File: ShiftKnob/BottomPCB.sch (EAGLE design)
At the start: 37 parts, among them IC2 7805DT, Q1 16MHz, Q2 MOSFET-NCHANNELSMD, Q3 MOSFET-PCHANNELSMD, Q4 MOSFET-NCHANNELSMD, Q5 MOSFET-NCHANNELSMD, Q6 MOSFET-NCHANNELSMD, U1 ATMEGA328

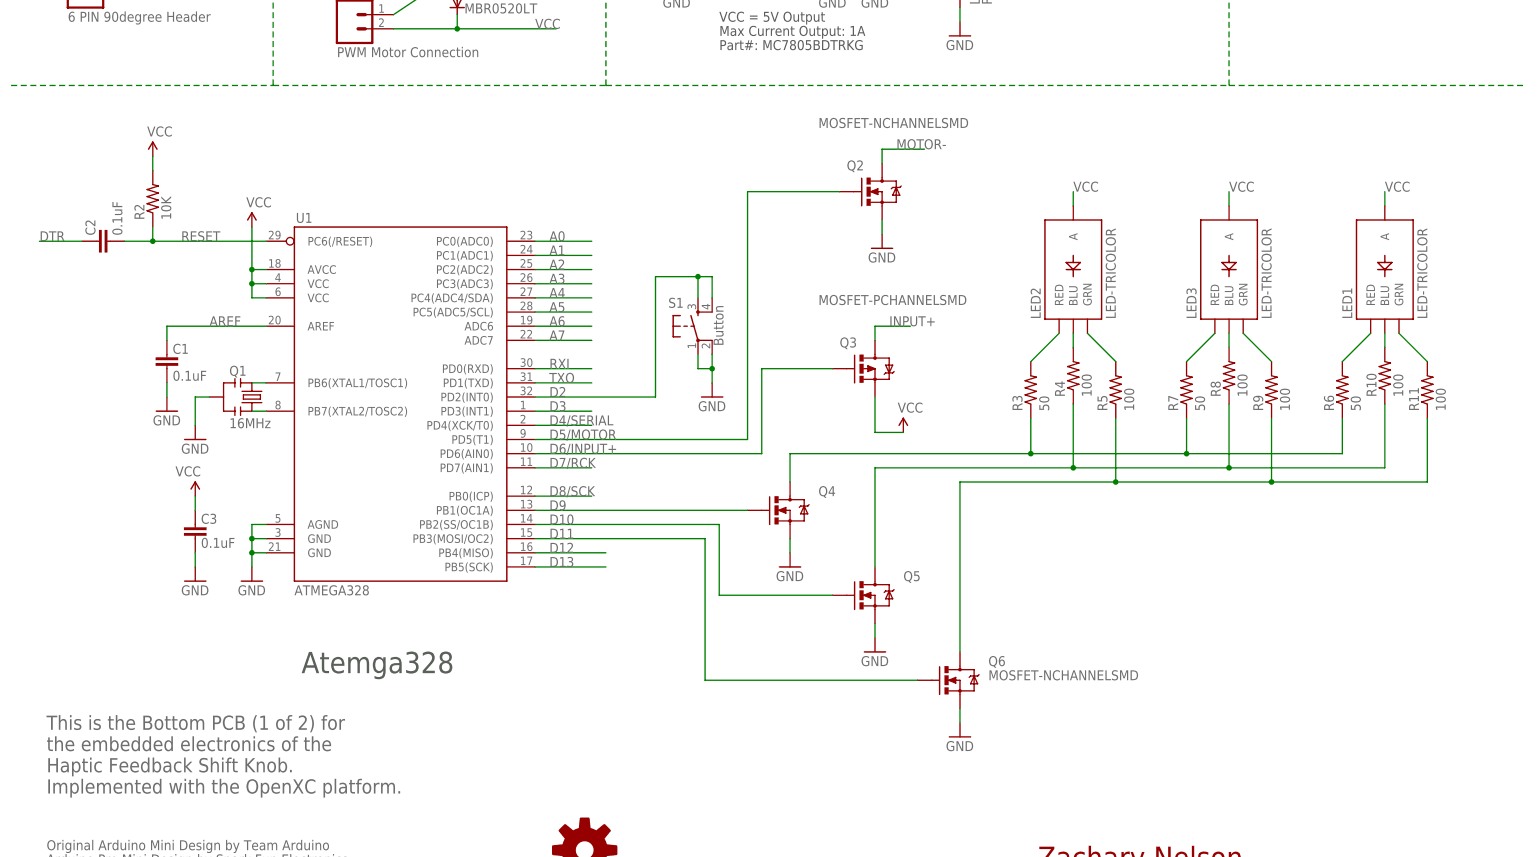
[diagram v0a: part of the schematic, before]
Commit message: add ICSP 6-pin header to schematic.
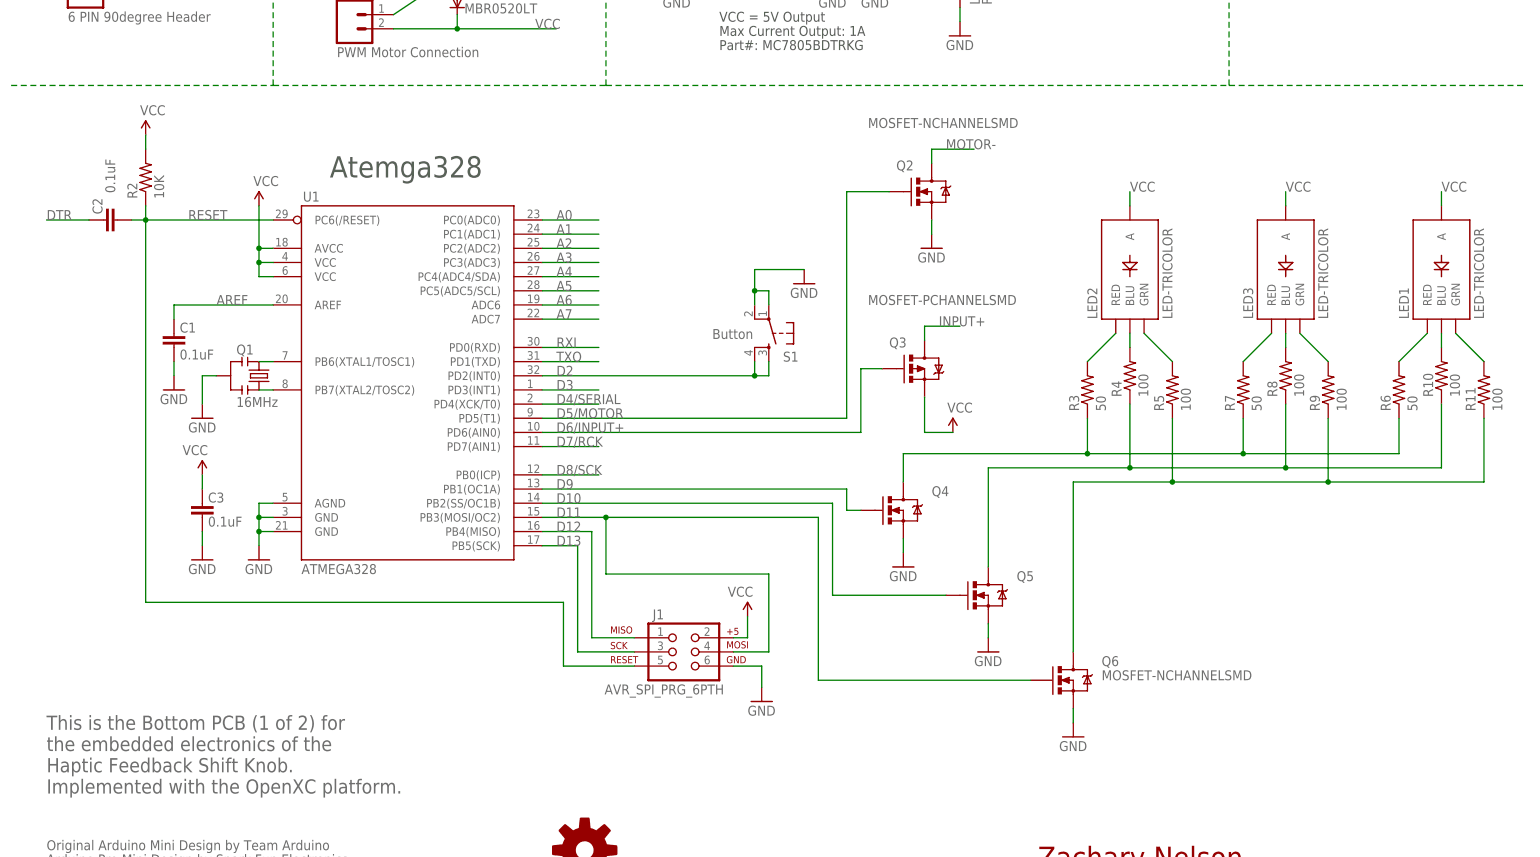
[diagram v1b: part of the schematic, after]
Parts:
- added J1: AVR_SPI_PRG_6PTH, SparkFun-Connectors:AVR_SPI_PRG_6PTH
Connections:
- net D12: now also J1.1
- net D13: now also J1.3
- net GND: now also J1.6
- net N$15: now also J1.4
- net RESET: now also J1.5
- net VCC: now also J1.2
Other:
- moved on the sheet: C1, C2, C3, LED1, LED2, LED3, Q1, Q2, Q3, Q4, Q5, Q6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

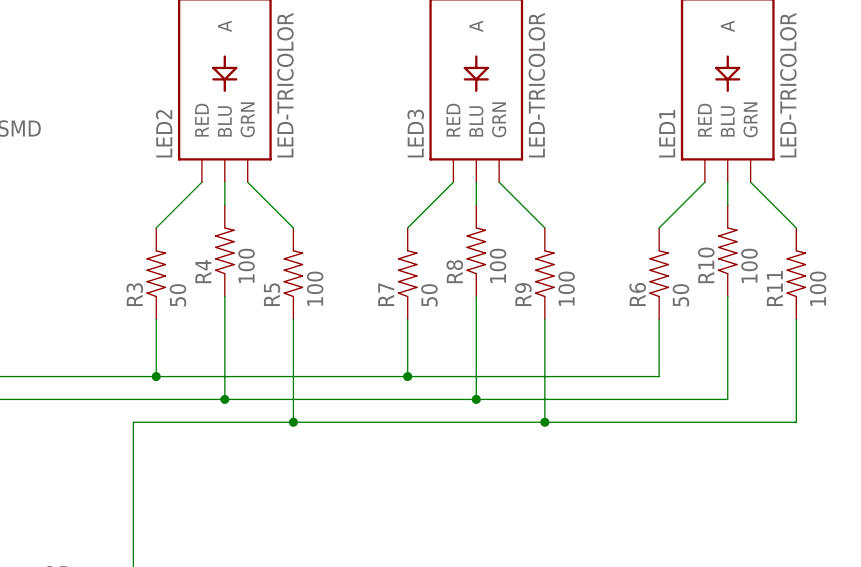
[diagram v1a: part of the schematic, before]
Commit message: change red LED resistance from 50ohm to 100ohm.
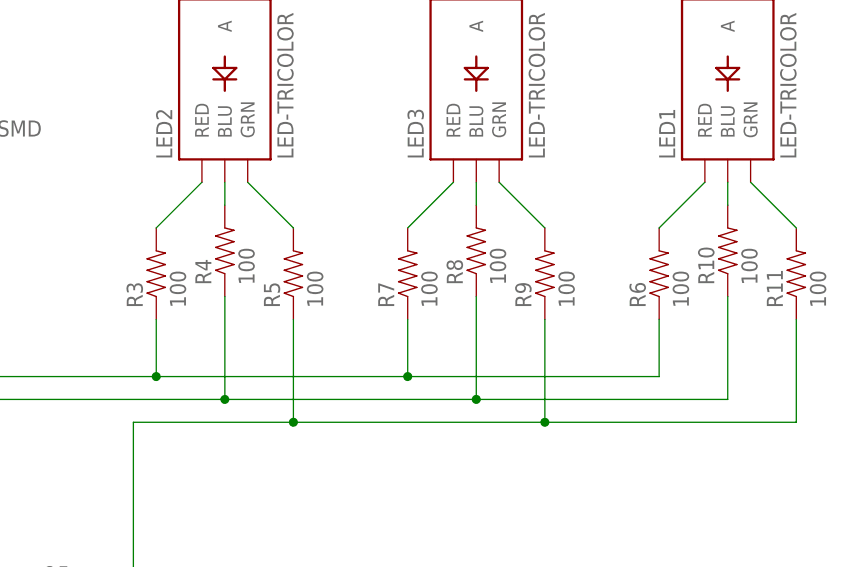
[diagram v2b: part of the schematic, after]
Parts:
- R3, R6, R7: value 50 -> 100
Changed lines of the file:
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@@
 <part name="GND11" library="SparkFun" deviceset="GND" device=""/>
 <part name="R4" library="SparkFun-Resistors" deviceset="RESISTOR" device="0805-RES" value="100"/>
-<part name="R3" library="SparkFun-Resistors" deviceset="RESISTOR" device="0805-RES" value="50"/>
+<part name="R3" library="SparkFun-Resistors" deviceset="RESISTOR" device="0805-RES" value="100"/>
 <part name="R5" library="SparkFun-Resistors" deviceset="RESISTOR" device="0805-RES" value="100"/>
-<part name="R7" library="SparkFun-Resistors" deviceset="RESISTOR" device="0805-RES" value="50"/>
+<part name="R7" library="SparkFun-Resistors" deviceset="RESISTOR" device="0805-RES" value="100"/>
 <part name="R8" library="SparkFun-Resistors" deviceset="RESISTOR" device="0805-RES" value="100"/>
 <part name="R9" library="SparkFun-Resistors" deviceset="RESISTOR" device="0805-RES" value="100"/>
@@
 <part name="D1" library="diode" deviceset="MBR0520LT" device=""/>
 <part name="LED1" library="SparkFun" deviceset="LED-TRICOLOR" device=""/>
-<part name="R6" library="SparkFun-Resistors" deviceset="RESISTOR" device="0805-RES" value="50"/>
+<part name="R6" library="SparkFun-Resistors" deviceset="RESISTOR" device="0805-RES" value="100"/>
 <part name="R10" library="SparkFun-Resistors" deviceset="RESISTOR" device="0805-RES" value="100"/>
 <part name="R11" library="SparkFun-Resistors" deviceset="RESISTOR" device="0805-RES" value="100"/>

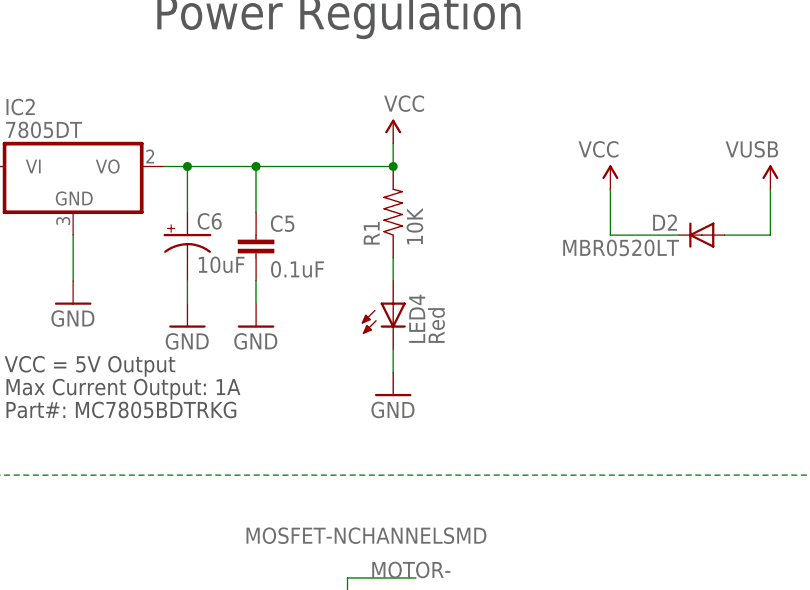
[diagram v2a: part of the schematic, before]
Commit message: remove power LED and resistor. not needed as RGB leds turn on when 5V is applied during startup.
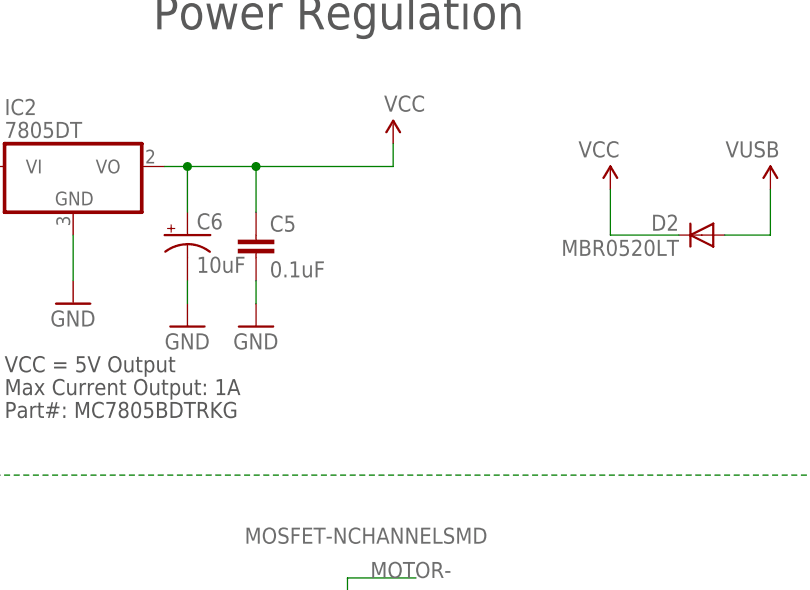
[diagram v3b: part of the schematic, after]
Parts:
- removed LED4: Red, SparkFun:LED0603
- removed R1: 10K, SparkFun:RESISTOR0402-RES
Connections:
- removed net N$3: LED4.A, R1.1
- net GND: no longer LED4.C
- net VCC: no longer R1.2
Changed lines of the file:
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@@
 <part name="GND9" library="SparkFun" deviceset="GND" device=""/>
 <part name="GND10" library="SparkFun" deviceset="GND" device=""/>
-<part name="R1" library="SparkFun" deviceset="RESISTOR" device="0402-RES" value="10K"/>
-<part name="LED4" library="SparkFun" deviceset="LED" device="0603" value="Red"/>
-<part name="GND11" library="SparkFun" deviceset="GND" device=""/>
 <part name="R4" library="SparkFun-Resistors" deviceset="RESISTOR" device="0805-RES" value="100"/>
 <part name="R3" library="SparkFun-Resistors" deviceset="RESISTOR" device="0805-RES" value="100"/>
@@
 <instance part="GND9" gate="1" x="151.13" y="170.18"/>
 <instance part="GND10" gate="1" x="158.75" y="170.18"/>
-<instance part="R1" gate="G$1" x="173.99" y="182.88" rot="R90"/>
-<instance part="LED4" gate="G$1" x="173.99" y="172.72"/>
-<instance part="GND11" gate="1" x="173.99" y="162.56"/>
 <instance part="R4" gate="G$1" x="204.47" y="101.6" rot="R90"/>
 <instance part="R3" gate="G$1" x="196.85" y="99.06" rot="R90"/>
@@
 </segment>
 <segment>
-<wire x1="173.99" y1="165.1" x2="173.99" y2="167.64" width="0.1524" layer="91"/>
-<pinref part="LED4" gate="G$1" pin="C"/>
-<pinref part="GND11" gate="1" pin="GND"/>
-</segment>
-<segment>
 <pinref part="Q4" gate="G$1" pin="S"/>
 <wire x1="163.83" y1="72.39" x2="163.83" y2="69.85" width="0.1524" layer="91"/>
@@
 <pinref part="C5" gate="G$1" pin="1"/>
 <junction x="158.75" y="187.96"/>
-<pinref part="R1" gate="G$1" pin="2"/>
-<junction x="173.99" y="187.96"/>
 </segment>
 <segment>
@@
 </segment>
 </net>
-<net name="N$3" class="0">
-<segment>
-<wire x1="173.99" y1="175.26" x2="173.99" y2="177.8" width="0.1524" layer="91"/>
-<pinref part="R1" gate="G$1" pin="1"/>
-<pinref part="LED4" gate="G$1" pin="A"/>
-</segment>
-</net>

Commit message: finish the schematic for the FTDI chip. Need to rework the board layout still.
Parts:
- removed JP2: FTDI Basic, SparkFun-Connectors:M06SIP
- added C10: 10uF, SparkFun:CAP_POL1206
- added C9: 0.1uF, SparkFun:CAP0402-CAP
- added LED6: Red, SparkFun:LED0603
- added LED7: Green, SparkFun:LED0603
- added R13, R14: 1K, SparkFun:RESISTOR0402-RES
- added U$6: USB-MINI-B_VERTICAL, FORD_frames:USB-MINI-B_VERTICAL
- added U3: FT232RL-BASICSSOP, SparkFun-DigitalIC:FT232RL-BASICSSOP
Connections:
- new net 5V: R13.2, R14.2
- new net N$21: U$6.D+, U3.USBDP
- new net N$22: U$6.D-, U3.USBDM
- new net N$23: LED6.A, R13.1
- new net N$24: LED7.A, R14.1
- new net RXLED1: LED7.C, U3.RXLED
- new net TXLED1: LED6.C, U3.TXLED
- net DTR: now also U3.DTR; no longer JP2.1
- net GND: now also C10.-, C9.2, U$6.GND, U3.AGND, U3.GND1, U3.GND2, U3.GND3, U3.TEST; no longer JP2.5, JP2.6
- net RXI: now also U3.RXD; no longer JP2.3
- net TXO: now also U3.TXD; no longer JP2.2
- net VUSB: now also C10.+, C9.1, U$6.VBUS, U3.VCC, U3.VCCIO; no longer JP2.4
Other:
- moved on the sheet: C4, C5, C6, D1, D2, IC2, JP1, JP3, JP4, LED1, LED2, LED3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

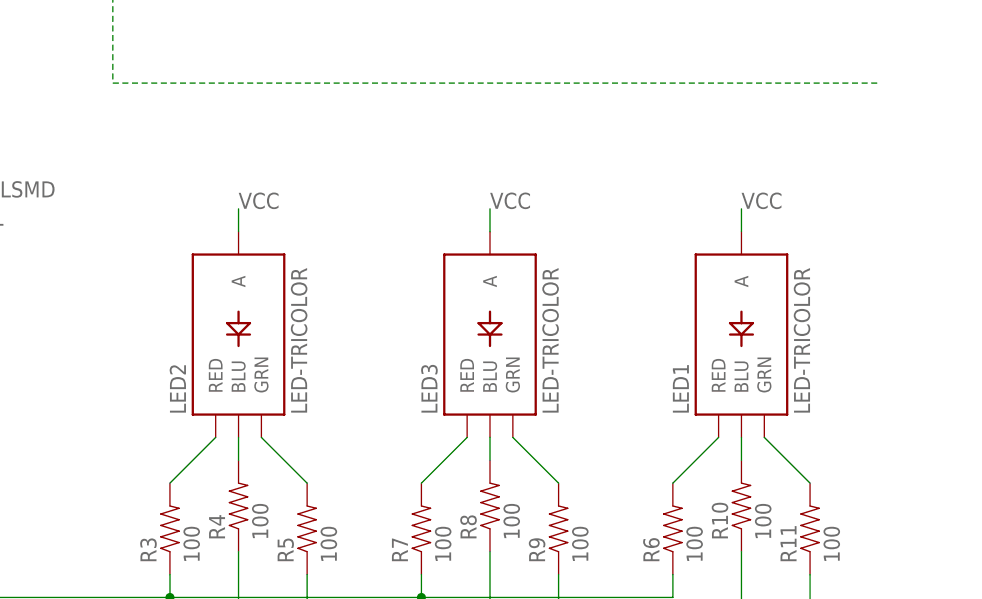
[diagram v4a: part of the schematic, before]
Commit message: switch out RGB LEDs for Right-Angle RGBs from FORD_frames library. Still need to fix layout.
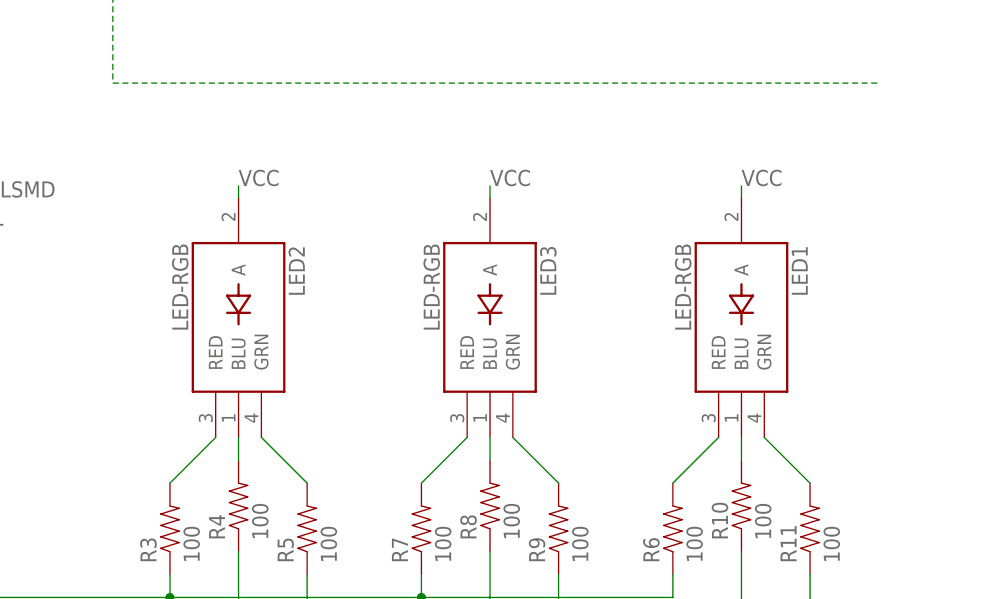
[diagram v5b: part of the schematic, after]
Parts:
- LED1, LED2, LED3: value LED-TRICOLOR -> LED-RGB; device SparkFun:LED-TRICOLOR -> FORD_frames:LED-RGB
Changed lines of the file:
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@@
 <setting verticaltext="up"/>
 </settings>
-<grid distance="0.05" unitdist="inch" unit="inch" style="lines" multiple="1" display="no" altdistance="0.01" altunitdist="inch" altunit="inch"/>
+<grid distance="0.1" unitdist="inch" unit="inch" style="lines" multiple="1" display="no" altdistance="0.01" altunitdist="inch" altunit="inch"/>
 <layers>
 <layer number="1" name="Top" color="4" fill="1" visible="no" active="no"/>
@@
 <attribute name="PROD_ID" value="CONN-08352"/>
 </part>
-<part name="LED2" library="SparkFun" deviceset="LED-TRICOLOR" device=""/>
-<part name="LED3" library="SparkFun" deviceset="LED-TRICOLOR" device=""/>
+<part name="LED2" library="FORD_frames" deviceset="LED-RGB" device=""/>
+<part name="LED3" library="FORD_frames" deviceset="LED-RGB" device=""/>
 <part name="VCC" library="SparkFun" deviceset="3.3V" device="" value="VCC"/>
 <part name="IC2" library="linear" deviceset="78*" device="DT" technology="05"/>
@@
 <part name="JP4" library="SparkFun-Connectors" deviceset="M02" device="-JST-2MM-SMT" value="PWM Motor Connection"/>
 <part name="D1" library="diode" deviceset="MBR0520LT" device=""/>
-<part name="LED1" library="SparkFun" deviceset="LED-TRICOLOR" device=""/>
+<part name="LED1" library="FORD_frames" deviceset="LED-RGB" device=""/>
 <part name="R6" library="SparkFun-Resistors" deviceset="RESISTOR" device="0805-RES" value="100"/>
 <part name="R10" library="SparkFun-Resistors" deviceset="RESISTOR" device="0805-RES" value="100"/>
@@
 <instance part="U$3" gate="G$1" x="106.68" y="16.51"/>
 <instance part="JP3" gate="G$1" x="57.15" y="185.42"/>
-<instance part="LED2" gate="G$1" x="201.93" y="97.79" rot="R90"/>
-<instance part="LED3" gate="G$1" x="229.87" y="97.79" rot="R90"/>
+<instance part="LED2" gate="G$1" x="204.47" y="100.33" rot="R270"/>
+<instance part="LED3" gate="G$1" x="232.41" y="100.33" rot="R270"/>
 <instance part="VCC" gate="G$1" x="152.4" y="190.5"/>
 <instance part="IC2" gate="A1" x="127" y="187.96"/>
@@
 <attribute name="VALUE" x="78.74" y="167.8686" size="1.778" layer="96"/>
 </instance>
-<instance part="LED1" gate="G$1" x="257.81" y="97.79" rot="R90"/>
+<instance part="LED1" gate="G$1" x="260.35" y="100.33" rot="R270"/>
 <instance part="R6" gate="G$1" x="252.73" y="77.47" rot="R90"/>
 <instance part="R10" gate="G$1" x="260.35" y="80.01" rot="R90"/>
@@
 <segment>
 <pinref part="LED2" gate="G$1" pin="A"/>
-<wire x1="204.47" y1="113.03" x2="204.47" y2="110.49" width="0.1524" layer="91"/>
-<label x="204.47" y="113.03" size="1.778" layer="95"/>
+<wire x1="204.47" y1="115.57" x2="204.47" y2="114.3" width="0.1524" layer="91"/>
+<label x="204.47" y="115.57" size="1.778" layer="95"/>
 </segment>
 <segment>
 <pinref part="LED3" gate="G$1" pin="A"/>
-<wire x1="232.41" y1="113.03" x2="232.41" y2="110.49" width="0.1524" layer="91"/>
-<label x="232.41" y="113.03" size="1.778" layer="95"/>
+<wire x1="232.41" y1="115.57" x2="232.41" y2="114.3" width="0.1524" layer="91"/>
+<label x="232.41" y="115.57" size="1.778" layer="95"/>
 </segment>
 <segment>
 <pinref part="LED1" gate="G$1" pin="A"/>
-<wire x1="260.35" y1="113.03" x2="260.35" y2="110.49" width="0.1524" layer="91"/>
-<label x="260.35" y="113.03" size="1.778" layer="95"/>
-</segment>
-<segment>
+<wire x1="260.35" y1="115.57" x2="260.35" y2="114.3" width="0.1524" layer="91"/>
+<label x="260.35" y="115.57" size="1.778" layer="95"/>
+</segment>
+<segment>

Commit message: add resistor arrays. clear off board layout and begin moving components.
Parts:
- removed C9: 0.1uF, SparkFun:CAP0402-CAP
- removed R10, R11, R3, R4, R5, R6, R7, R8, R9: 100, SparkFun-Resistors:RESISTOR0805-RES
- added RN1, RN2: 150, resistor-dil:4R-NEXBS8V
- added RN3: 100, resistor-dil:4R-NEXBS8V
- C4: value 10uF -> 0.1uF; device SparkFun:CAP_POL1206 -> SparkFun:CAP0402-CAP
- IC2: value 7805DT -> UA78M05DCY; device linear:7805DT -> linear:UA78M05DCY
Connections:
- net D10: now also RN3A.1, RN3B.1, RN3C.1; no longer R10.1, R4.1, R8.1
- net D11: now also RN2A.1, RN2B.1, RN2C.1; no longer R11.1, R5.1, R9.1
- net D9: now also RN1A.1, RN1B.1, RN1C.1; no longer R3.1, R6.1, R7.1
- net GND: now also C4.1, IC2.GND@1; no longer C4.-, C9.2
- net N$10: now also RN2C.2; no longer R11.2
- net N$16: now also RN3B.2; no longer R8.2
- net N$25: now also RN3A.2; no longer R4.2
- net N$4: now also RN1A.2; no longer R3.2
- net N$5: now also RN2A.2; no longer R5.2
- net N$6: now also RN1B.2; no longer R7.2
- net N$7: now also RN3C.2; no longer R10.2
- net N$8: now also RN2B.2; no longer R9.2
- net N$9: now also RN1C.2; no longer R6.2
- net RAW: no longer C4.+
- net VUSB: now also C4.2; no longer C9.1
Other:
- note added: "Spare Resistors"
- moved on the sheet: C10, C3, C5, C6, D2, LED6, LED7, Q2, R13, R14, R2, U3

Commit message: bring up to date. schematic almost finalized.
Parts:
- JP3: value 12V Battery Connection -> 12V Vehicle Connection
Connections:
- net RAW renamed 12V
- removed net 5V: R13.2, R14.2
- new net 3.3V: LED1.A, LED2.A, LED3.A
- net VCC: no longer LED1.A, LED2.A, LED3.A
- net VUSB: now also R13.2, R14.2
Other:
- moved on the sheet: C10, C4, D2, IC2, LED6, LED7, R13, R14, U3
